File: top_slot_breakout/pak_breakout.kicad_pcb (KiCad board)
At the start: 2 copper layers, 132 x 100 mm, 31 parts, among them J1 Conn_02x08_Odd_Even, J10 Conn_01x10_Female, J11 Conn_01x06_Female, J12 Conn_01x10_Female, J13 Conn_01x10_Female, J14 Conn_01x06_Female, J2 Conn_01x06_Female, J3 Conn_01x04_Female, J4 Conn_01x02_Female, J5 Conn_01x03_Female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

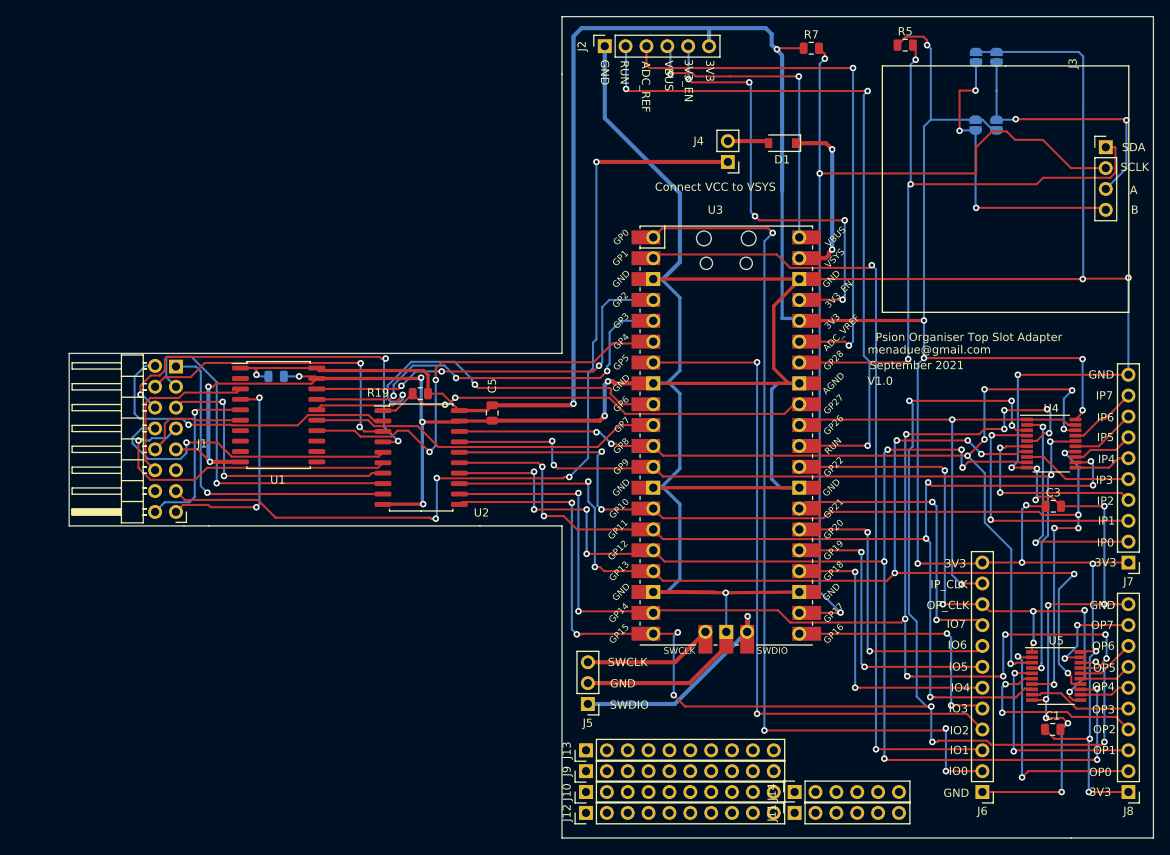
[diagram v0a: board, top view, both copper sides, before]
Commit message: Added code based on (identical to) pak-gadget
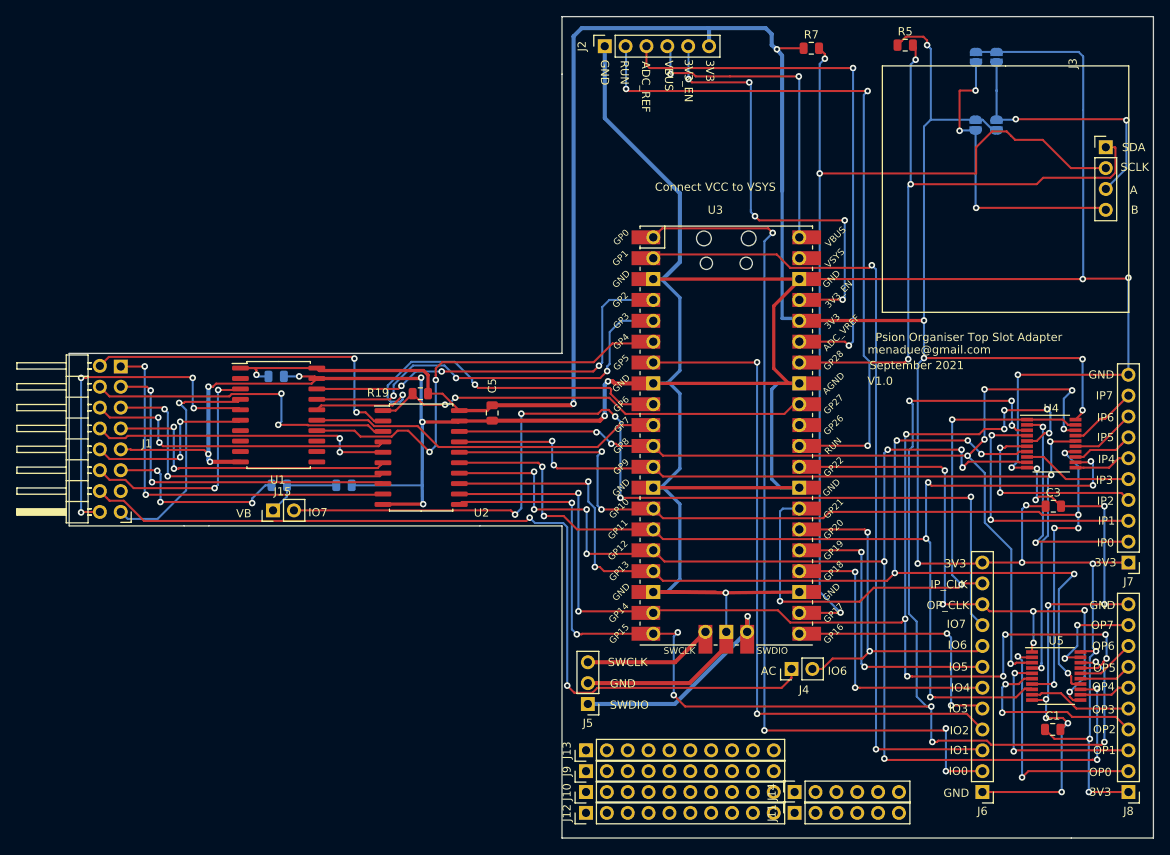
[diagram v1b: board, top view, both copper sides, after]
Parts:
- removed D1: D_Schottky, Diode_SMD:D_SOD-123
- added J15: Conn_01x02_Male, Connector_PinHeader_2.54mm:PinHeader_1x02_P2.54mm_Vertical, F.Cu at (337.8, 245.1)
- added R1: R_Small, Resistor_SMD:R_0805_2012Metric, B.Cu at (338.6, 242.1)
- added R2: R_Small, Resistor_SMD:R_0805_2012Metric, B.Cu at (346.5, 242.1)
- J4: value Conn_01x02_Female -> Conn_01x02_Male
- moved J4 62.2 mm to (400.9, 264.4), turned to 90 degrees
- moved J1 6.72 mm to (319.3, 245.3)
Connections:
- J1 pad 11: (no net) -> VB
- J1 pad 13: VCC -> (no net)
- J1 pad 14: (no net) -> AC
- J4 pad 1: VCC -> AC
- J4 pad 2: Net-(D1-Pad2) -> IO6
- U3 pad 27: IO7 -> IP_CLK
- U3 pad 31: IP_CLK -> Net-(U3-Pad31)
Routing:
- net VCC: track 110.0 -> 0.00 mm, vias 4 -> 0
- net AC: track 0.00 -> 107.9 mm, vias 0 -> 2
- net IO7: track 36.9 -> 120.8 mm, vias 2 -> 5
- net VB: track 0.00 -> 23.3 mm, vias 0 -> 3
- net Net-(U3-Pad39): track 21.5 -> 0.00 mm, vias 2 -> 0
- net SMR: track 21.6 -> 41.9 mm, vias 1 -> 4
- net IP_CLK: track 57.3 -> 74.8 mm, vias 2 -> 3
- net GND: track 518.1 -> 532.9 mm, vias 22 -> 23
- net SD2: track 48.5 -> 38.3 mm, vias 3 -> 2
- net Net-(J15-Pad1): track 0.00 -> 10.1 mm
- net SCLK: track 13.1 -> 22.1 mm, vias 0 -> 2
- net SS: track 20.9 -> 29.8 mm, vias 0 -> 2
- net IO6: track 37.0 -> 44.9 mm
- net SD7: track 39.8 -> 47.5 mm, vias 1 -> 2
- net SD5: track 34.6 -> 40.1 mm
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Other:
- board text added: "AC"
- board text added: "VB"
